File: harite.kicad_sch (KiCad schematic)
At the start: 39 parts, among them U1 RP2040_Zero

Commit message: Fix usb
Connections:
- net 5V: now also USB1.11 (VBUS)
- net GP0: now also USB1.7 (DN1); no longer USB1.6 (DP1)
- net GP1: now also USB1.6 (DP1); no longer USB1.7 (DN1)
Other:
- moved on the sheet: USB1
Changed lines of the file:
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@@
 		)
 	)
+	(global_label "5V"
+		(shape input)
+		(at 328.93 87.63 180)
+		(fields_autoplaced yes)
+		(effects
+			(font
+				(size 1.27 1.27)
+			)
+			(justify right)
+		)
+		(property "Intersheetrefs" "${INTERSHEET_REFS}"
+			(at 323.6467 87.63 0)
+			(effects
+				(font
+					(size 1.27 1.27)
+				)
+				(justify right)
+				(hide yes)
+			)
+		)
+	)
 	(global_label "SI"
 		(shape input)
@@
 		)
 	)
-	(global_label "GP0"
-		(shape input)
-		(at 345.44 101.6 0)
-		(fields_autoplaced yes)
-		(effects
-			(font
-				(size 1.27 1.27)
-			)
-			(justify left)
-		)
-		(property "Intersheetrefs" "${INTERSHEET_REFS}"
-			(at 352.1747 101.6 0)
-			(effects
-				(font
-					(size 1.27 1.27)
-				)
-				(justify left)
-				(hide yes)
-			)
-		)
-	)
 	(global_label "Row 1"
 		(shape input)
@@
 		)
 	)
-	(global_label "GP1"
-		(shape input)
-		(at 345.44 104.14 0)
-		(fields_autoplaced yes)
-		(effects
-			(font
-				(size 1.27 1.27)
-			)
-			(justify left)
-		)
-		(property "Intersheetrefs" "${INTERSHEET_REFS}"
-			(at 352.1747 104.14 0)
-			(effects
-				(font
-					(size 1.27 1.27)
-				)
-				(justify left)
-				(hide yes)
-			)
-		)
-	)
 	(global_label "GND"
 		(shape input)
-		(at 345.44 88.9 0)
+		(at 328.93 113.03 180)
 		(fields_autoplaced yes)
 		(effects
@@
 				(size 1.27 1.27)
 			)
-			(justify left)
+			(justify right)
 		)
 		(property "Intersheetrefs" "${INTERSHEET_REFS}"
-			(at 352.2957 88.9 0)
+			(at 322.0743 113.03 0)
 			(effects
 				(font
 					(size 1.27 1.27)
 				)
-				(justify left)
+				(justify right)
 				(hide yes)
 			)
@@
 	(global_label "5V"
 		(shape input)
-		(at 345.44 91.44 0)
+		(at 328.93 110.49 180)
 		(fields_autoplaced yes)
 		(effects
@@
 				(size 1.27 1.27)
 			)
-			(justify left)
+			(justify right)
 		)
 		(property "Intersheetrefs" "${INTERSHEET_REFS}"
-			(at 350.7233 91.44 0)
+			(at 323.6467 110.49 0)
 			(effects
 				(font
 					(size 1.27 1.27)
 				)
-				(justify left)
+				(justify right)
 				(hide yes)
 			)
@@
 	(global_label "GND"
 		(shape input)
-		(at 345.44 116.84 0)
+		(at 328.93 85.09 180)
 		(fields_autoplaced yes)
 		(effects
@@
 				(size 1.27 1.27)
 			)
-			(justify left)
+			(justify right)
 		)
 		(property "Intersheetrefs" "${INTERSHEET_REFS}"
-			(at 352.2957 116.84 0)
+			(at 322.0743 85.09 0)
 			(effects
 				(font
 					(size 1.27 1.27)
 				)
-				(justify left)
+				(justify right)
 				(hide yes)
 			)
@@
 	(global_label "GP0"
 		(shape input)
-		(at 345.44 99.06 0)
+		(at 328.93 102.87 180)
 		(fields_autoplaced yes)
 		(effects
@@
 				(size 1.27 1.27)
 			)
-			(justify left)
+			(justify right)
 		)
 		(property "Intersheetrefs" "${INTERSHEET_REFS}"
-			(at 352.1747 99.06 0)
+			(at 322.1953 102.87 0)
 			(effects
 				(font
 					(size 1.27 1.27)
 				)
-				(justify left)
+				(justify right)
 				(hide yes)
 			)
@@
 	(global_label "GND"
 		(shape input)
-		(at 345.44 119.38 0)
+		(at 328.93 82.55 180)
 		(fields_autoplaced yes)
 		(effects
@@
 				(size 1.27 1.27)
 			)
-			(justify left)
+			(justify right)
 		)
 		(property "Intersheetrefs" "${INTERSHEET_REFS}"
-			(at 352.2957 119.38 0)
+			(at 322.0743 82.55 0)
 			(effects
 				(font
 					(size 1.27 1.27)
 				)
-				(justify left)
+				(justify right)
 				(hide yes)
 			)
@@
 		)
 	)
-	(global_label "GP1"
+	(global_label "Row 3"
 		(shape input)
-		(at 345.44 106.68 0)
+		(at 275.59 185.42 180)
 		(fields_autoplaced yes)
 		(effects
@@
 				(size 1.27 1.27)
 			)
-			(justify left)
+			(justify right)
 		)
 		(property "Intersheetrefs" "${INTERSHEET_REFS}"
-			(at 352.1747 106.68 0)
+			(at 266.6782 185.42 0)
 			(effects
 				(font
 					(size 1.27 1.27)
 				)
-				(justify left)
+				(justify right)
 				(hide yes)
 			)
 		)
 	)
-	(global_label "Row 3"
+	(global_label "Row 2"
 		(shape input)
-		(at 275.59 185.42 180)
+		(at 275.59 182.88 180)
 		(fields_autoplaced yes)
 		(effects
@@
 		)
 		(property "Intersheetrefs" "${INTERSHEET_REFS}"
-			(at 266.6782 185.42 0)
+			(at 266.6782 182.88 0)
 			(effects
 				(font
@@
 		)
 	)
-	(global_label "Row 2"
+	(global_label "Row 4"
 		(shape input)
-		(at 275.59 182.88 180)
+		(at 71.12 55.88 0)
 		(fields_autoplaced yes)
 		(effects
@@
 				(size 1.27 1.27)
 			)
-			(justify right)
+			(justify left)
 		)
 		(property "Intersheetrefs" "${INTERSHEET_REFS}"
-			(at 266.6782 182.88 0)
+			(at 80.0318 55.88 0)
 			(effects
 				(font
 					(size 1.27 1.27)
 				)
-				(justify right)
+				(justify left)
 				(hide yes)
 			)
 		)
 	)
-	(global_label "Row 4"
+	(global_label "GP1"
 		(shape input)
-		(at 71.12 55.88 0)
+		(at 328.93 100.33 180)
 		(fields_autoplaced yes)
 		(effects
@@
 				(size 1.27 1.27)
 			)
-			(justify left)
+			(justify right)
 		)
 		(property "Intersheetrefs" "${INTERSHEET_REFS}"
-			(at 80.0318 55.88 0)
+			(at 322.1953 100.33 0)
 			(effects
 				(font
 					(size 1.27 1.27)
 				)
-				(justify left)
+				(justify right)
 				(hide yes)
 			)
@@
 		)
 	)
+	(global_label "GP0"
+		(shape input)
+		(at 328.93 97.79 180)
+		(fields_autoplaced yes)
+		(effects
+			(font
+				(size 1.27 1.27)
+			)
+			(justify right)
+		)
+		(property "Intersheetrefs" "${INTERSHEET_REFS}"
+			(at 322.1953 97.79 0)
+			(effects
+				(font
+					(size 1.27 1.27)
+				)
+				(justify right)
+				(hide yes)
+			)
+		)
+	)
 	(global_label "Row 4"
 		(shape input)
@@
 		)
 	)
+	(global_label "GP1"
+		(shape input)
+		(at 328.93 95.25 180)
+		(fields_autoplaced yes)
+		(effects
+			(font
+				(size 1.27 1.27)
+			)
+			(justify right)
+		)
+		(property "Intersheetrefs" "${INTERSHEET_REFS}"
+			(at 322.1953 95.25 0)
+			(effects
+				(font
+					(size 1.27 1.27)
+				)
+				(justify right)
+				(hide yes)
+			)
+		)
+	)
 	(global_label "Col 3"
 		(shape input)
@@
 	(symbol
 		(lib_id "USBType-C:HRO-TYPE-C-31-M-12")
-		(at 342.9 102.87 0)
+		(at 331.47 99.06 180)
 		(unit 1)
 		(exclude_from_sim no)
@@
 		(fields_autoplaced yes)
 		(property "Reference" "USB1"
-			(at 337.185 82.55 0)
+			(at 337.185 119.38 0)
 			(effects
 				(font
@@
 		)
 		(property "Value" "HRO-TYPE-C-31-M-12"
-			(at 337.185 85.09 0)
+			(at 337.185 116.84 0)
 			(effects
 				(font
@@
 		)
 		(property "Footprint" "footprints:HRO-TYPE-C-31-M-12"
-			(at 342.9 102.87 0)
+			(at 331.47 99.06 0)
 			(effects
 				(font
@@
 		)
 		(property "Datasheet" ""
-			(at 342.9 102.87 0)
+			(at 331.47 99.06 0)
 			(effects
 				(font
@@
 		)
 		(property "Description" ""
-			(at 342.9 102.87 0)
+			(at 331.47 99.06 0)
 			(effects
 				(font

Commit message: Shaping
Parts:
- removed D26, D27, D28, D29, D30: D, ScottoKeebs_Components:Diode_SOD-123, symbol Device:D
- removed S6: SKRHADE010, footprints:SKRHADE010, symbol SKRHADE010:SKRHADE010
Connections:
- net Col 6 is gone; now on net Col 5: U1.14 (13)
- net Col 1: now also U1.10 (9); no longer U1.9 (8)
- net Col 2: now also U1.11 (10); no longer U1.10 (9)
- net Col 3: now also U1.12 (11); no longer U1.11 (10)
- net Col 4: now also U1.13 (12); no longer U1.12 (11)
- net Col 5: no longer U1.13 (12)
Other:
- moved on the sheet: Cirque1, D21, D22, D23, D24, D25, S5, USB1

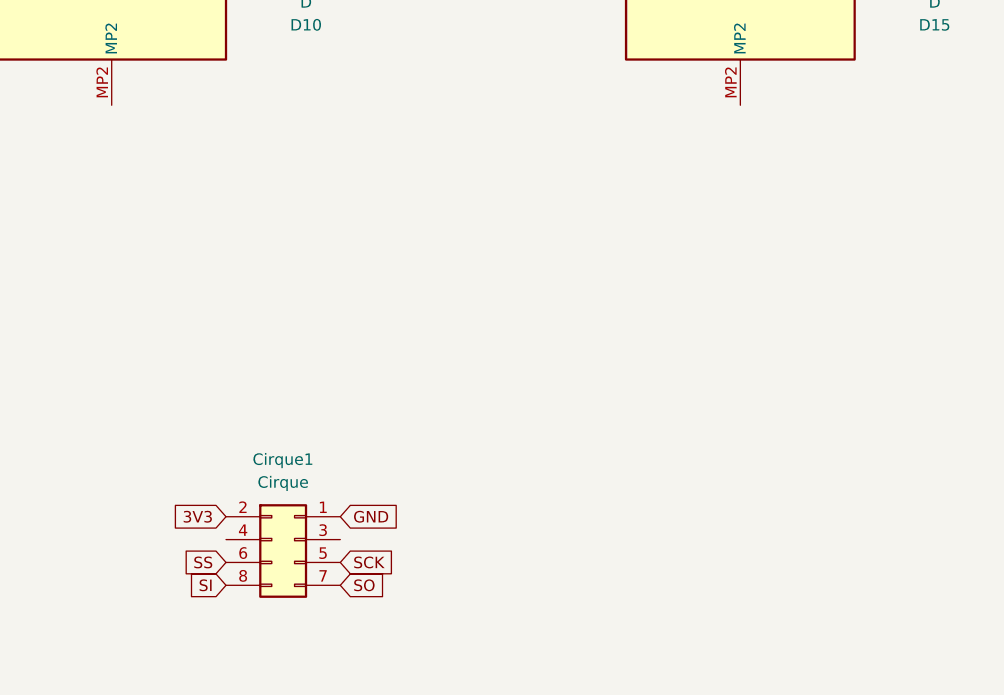
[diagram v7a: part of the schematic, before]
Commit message: Add cirque connector
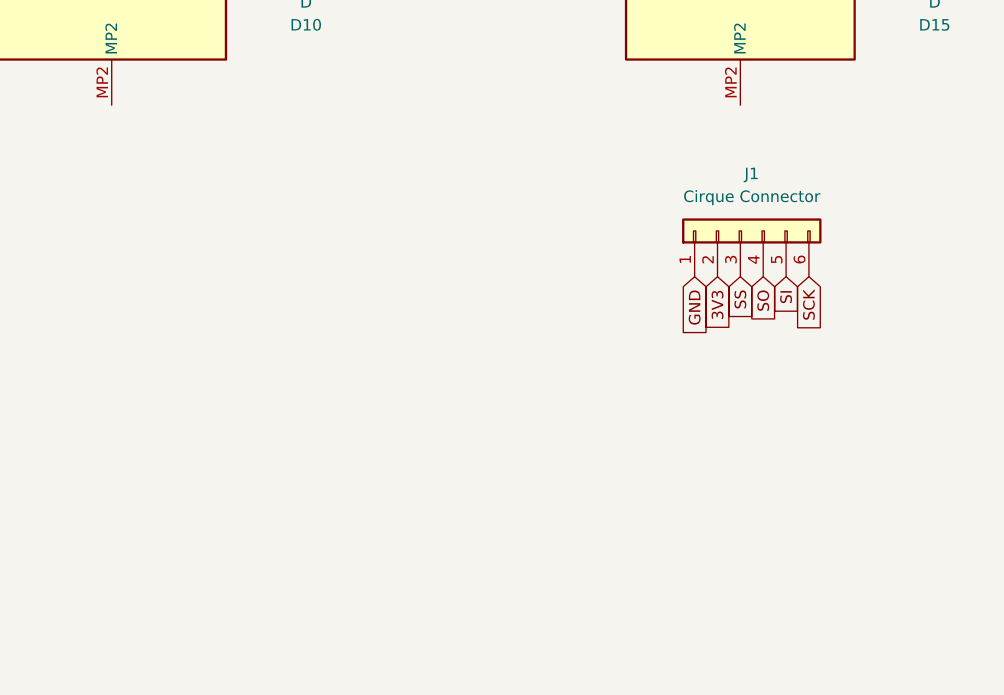
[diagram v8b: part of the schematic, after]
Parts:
- removed Cirque1: Cirque, footprints:CIRQUE-TM040040, symbol Connector_Generic:Conn_02x04_Top_Bottom
- added J1: Cirque Connector, footprints:Cirque-connector, symbol Connector_Generic:Conn_01x06
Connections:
- net 3V3: now also J1.2 (Pin_2)
- net GND: now also J1.1 (Pin_1)
- net SCK: now also J1.6 (Pin_6)
- net SI: now also J1.5 (Pin_5)
- net SO: now also J1.4 (Pin_4)
- net SS: now also J1.3 (Pin_3)
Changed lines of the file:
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@@
 		)
 	)
-	(global_label "SI"
+	(global_label "3V3"
 		(shape input)
-		(at 128.27 129.54 180)
+		(at 182.88 95.25 270)
 		(fields_autoplaced yes)
 		(effects
@@
 		)
 		(property "Intersheetrefs" "${INTERSHEET_REFS}"
-			(at 123.4705 129.54 0)
+			(at 182.88 101.7428 90)
 			(effects
 				(font
@@
 		)
 	)
-	(global_label "SO"
-		(shape input)
-		(at 140.97 129.54 0)
-		(fields_autoplaced yes)
-		(effects
-			(font
-				(size 1.27 1.27)
-			)
-			(justify left)
-		)
-		(property "Intersheetrefs" "${INTERSHEET_REFS}"
-			(at 146.4952 129.54 0)
-			(effects
-				(font
-					(size 1.27 1.27)
-				)
-				(justify left)
-				(hide yes)
-			)
-		)
-	)
 	(global_label "Row 4"
 		(shape input)
@@
 		)
 	)
-	(global_label "Row 2"
+	(global_label "SI"
 		(shape input)
-		(at 229.87 58.42 180)
+		(at 190.5 95.25 270)
 		(fields_autoplaced yes)
 		(effects
@@
 		)
 		(property "Intersheetrefs" "${INTERSHEET_REFS}"
-			(at 220.9582 58.42 0)
+			(at 190.5 100.0495 90)
 			(effects
 				(font
@@
 		)
 	)
-	(global_label "Row 1"
+	(global_label "Row 2"
 		(shape input)
-		(at 229.87 55.88 180)
+		(at 229.87 58.42 180)
 		(fields_autoplaced yes)
 		(effects
@@
 		)
 		(property "Intersheetrefs" "${INTERSHEET_REFS}"
-			(at 220.9582 55.88 0)
+			(at 220.9582 58.42 0)
 			(effects
 				(font
@@
 		)
 	)
-	(global_label "SS"
+	(global_label "Row 1"
 		(shape input)
-		(at 128.27 127 180)
+		(at 229.87 55.88 180)
 		(fields_autoplaced yes)
 		(effects
@@
 		)
 		(property "Intersheetrefs" "${INTERSHEET_REFS}"
-			(at 122.8658 127 0)
+			(at 220.9582 55.88 0)
 			(effects
 				(font
@@
 		)
 	)
-	(global_label "SCK"
-		(shape input)
-		(at 140.97 127 0)
-		(fields_autoplaced yes)
-		(effects
-			(font
-				(size 1.27 1.27)
-			)
-			(justify left)
-		)
-		(property "Intersheetrefs" "${INTERSHEET_REFS}"
-			(at 147.7047 127 0)
-			(effects
-				(font
-					(size 1.27 1.27)
-				)
-				(justify left)
-				(hide yes)
-			)
-		)
-	)
 	(global_label "Col 1"
 		(shape input)
@@
 		)
 	)
-	(global_label "GND"
+	(global_label "SS"
 		(shape input)
-		(at 140.97 121.92 0)
+		(at 185.42 95.25 270)
 		(fields_autoplaced yes)
 		(effects
@@
 				(size 1.27 1.27)
 			)
-			(justify left)
+			(justify right)
 		)
 		(property "Intersheetrefs" "${INTERSHEET_REFS}"
-			(at 147.8257 121.92 0)
+			(at 185.42 100.6542 90)
 			(effects
 				(font
 					(size 1.27 1.27)
 				)
-				(justify left)
+				(justify right)
 				(hide yes)
 			)
@@
 		)
 	)
+	(global_label "GND"
+		(shape input)
+		(at 180.34 95.25 270)
+		(fields_autoplaced yes)
+		(effects
+			(font
+				(size 1.27 1.27)
+			)
+			(justify right)
+		)
+		(property "Intersheetrefs" "${INTERSHEET_REFS}"
+			(at 180.34 102.1057 90)
+			(effects
+				(font
+					(size 1.27 1.27)
+				)
+				(justify right)
+				(hide yes)
+			)
+		)
+	)
 	(global_label "Row 4"
 		(shape input)
@@
 		)
 	)
+	(global_label "SCK"
+		(shape input)
+		(at 193.04 95.25 270)
+		(fields_autoplaced yes)
+		(effects
+			(font
+				(size 1.27 1.27)
+			)
+			(justify right)
+		)
+		(property "Intersheetrefs" "${INTERSHEET_REFS}"
+			(at 193.04 101.9847 90)
+			(effects
+				(font
+					(size 1.27 1.27)
+				)
+				(justify right)
+				(hide yes)
+			)
+		)
+	)
 	(global_label "Col 3"
 		(shape input)
@@
 		)
 	)
-	(global_label "3V3"
+	(global_label "SO"
 		(shape input)
-		(at 128.27 121.92 180)
+		(at 187.96 95.25 270)
 		(fields_autoplaced yes)
 		(effects
@@
 		)
 		(property "Intersheetrefs" "${INTERSHEET_REFS}"
-			(at 121.7772 121.92 0)
+			(at 187.96 100.7752 90)
 			(effects
 				(font
@@
 	)
 	(symbol
+		(lib_id "Connector_Generic:Conn_01x06")
+		(at 185.42 90.17 90)
+		(unit 1)
+		(exclude_from_sim no)
+		(in_bom yes)
+		(on_board yes)
+		(dnp no)
+		(fields_autoplaced yes)
+		(property "Reference" "J1"
+			(at 186.69 83.82 90)
+			(effects
+				(font
+					(size 1.27 1.27)
+				)
+			)
+		)
+		(property "Value" "Cirque Connector"
+			(at 186.69 86.36 90)
+			(effects
+				(font
+					(size 1.27 1.27)
+				)
+			)
+		)
+		(property "Footprint" "footprints:Cirque-connector"
+			(at 185.42 90.17 0)
+			(effects
+				(font
+					(size 1.27 1.27)
+				)
+				(hide yes)
+			)
+		)
+		(property "Datasheet" "~"
+			(at 185.42 90.17 0)
+			(effects
+				(font
+					(size 1.27 1.27)
+				)
+				(hide yes)
+			)
+		)
+		(property "Description" "Generic connector, single row, 01x06, script generated (kicad-library-utils/schlib/autogen/connector/)"
+			(at 185.42 90.17 0)
+			(effects
+				(font
+					(size 1.27 1.27)
+				)
+				(hide yes)
+			)
+		)
+		(pin "6"
+		)
+		(pin "5"
+		)
+		(pin "2"
+		)
+		(pin "4"
+		)
+		(pin "3"
+		)
+		(pin "1"
+		)
+		(instances
+			(project "harite"
+				(path "/feb70c3f-3e34-4f8f-9694-07d231f2d237"
+					(reference "J1")
+					(unit 1)
+				)
+			)
+		)
+	)
+	(symbol
 		(lib_id "USBType-C:HRO-TYPE-C-31-M-12")
 		(at 318.77 114.3 180)
@@
 					(unit 1)
 				)
-			)
-		)
-	)
-	(symbol
-		(lib_id "Connector_Generic:Conn_02x04_Top_Bottom")
-		(at 133.35 124.46 0)
-		(unit 1)
-		(exclude_from_sim no)
-		(in_bom yes)
-		(on_board yes)
-		(dnp no)
-		(fields_autoplaced yes)
-		(property "Reference" "Cirque1"
-			(at 134.62 115.57 0)
-			(effects
-				(font
-					(size 1.27 1.27)
-				)
-			)
-		)
-		(property "Value" "Cirque"
-			(at 134.62 118.11 0)
-			(effects
-				(font
-					(size 1.27 1.27)
-				)
-			)
-		)
-		(property "Footprint" "footprints:CIRQUE-TM040040"
-			(at 133.35 124.46 0)
-			(effects
-				(font
-					(size 1.27 1.27)
-				)
-				(hide yes)
-			)
-		)
-		(property "Datasheet" "~"
-			(at 133.35 124.46 0)
-			(effects
-				(font
-					(size 1.27 1.27)
-				)
-				(hide yes)
-			)
-		)
-		(property "Description" "Generic connector, double row, 02x04, top/bottom pin numbering scheme (row 1: 1...pins_per_row, row2: pins_per_row+1 ... num_pins), script generated (kicad-library-utils/schlib/autogen/connector/)"
-			(at 133.35 124.46 0)
-			(effects
-				(font
-					(size 1.27 1.27)
-				)
-				(hide yes)
-			)
-		)
-		(pin "8"
-		)
-		(pin "5"
-		)
-		(pin "1"
-		)
-		(pin "4"
-		)
-		(pin "3"
-		)
-		(pin "2"
-		)
-		(pin "6"
-		)
-		(pin "7"
-		)
-		(instances
-			(project "harite"
-				(path "/feb70c3f-3e34-4f8f-9694-07d231f2d237"
-					(reference "Cirque1")
-					(unit 1)
-				)
